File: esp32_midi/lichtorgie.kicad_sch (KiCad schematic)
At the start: 64 parts

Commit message: Updated pcb
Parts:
- renumbered D26 to D?

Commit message: Started work on PCB
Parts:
- added D? (x8): WS2812B, LED_SMD:LED_WS2812B_PLCC4_5.0x5.0mm_P3.2mm, symbol LED:WS2812B
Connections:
- net VDD: now also D?.1 (VDD), D?.1 (VDD), D?.1 (VDD), D?.1 (VDD), D?.1 (VDD), D?.1 (VDD), D?.1 (VDD), D?.1 (VDD)
- net VSS: now also D?.3 (VSS), D?.3 (VSS), D?.3 (VSS), D?.3 (VSS), D?.3 (VSS), D?.3 (VSS), D?.3 (VSS), D?.3 (VSS)
- net at D?.2 (DOUT): now also D?.4 (DIN)
- new net: D?.2 (DOUT), D?.4 (DIN) (x7)

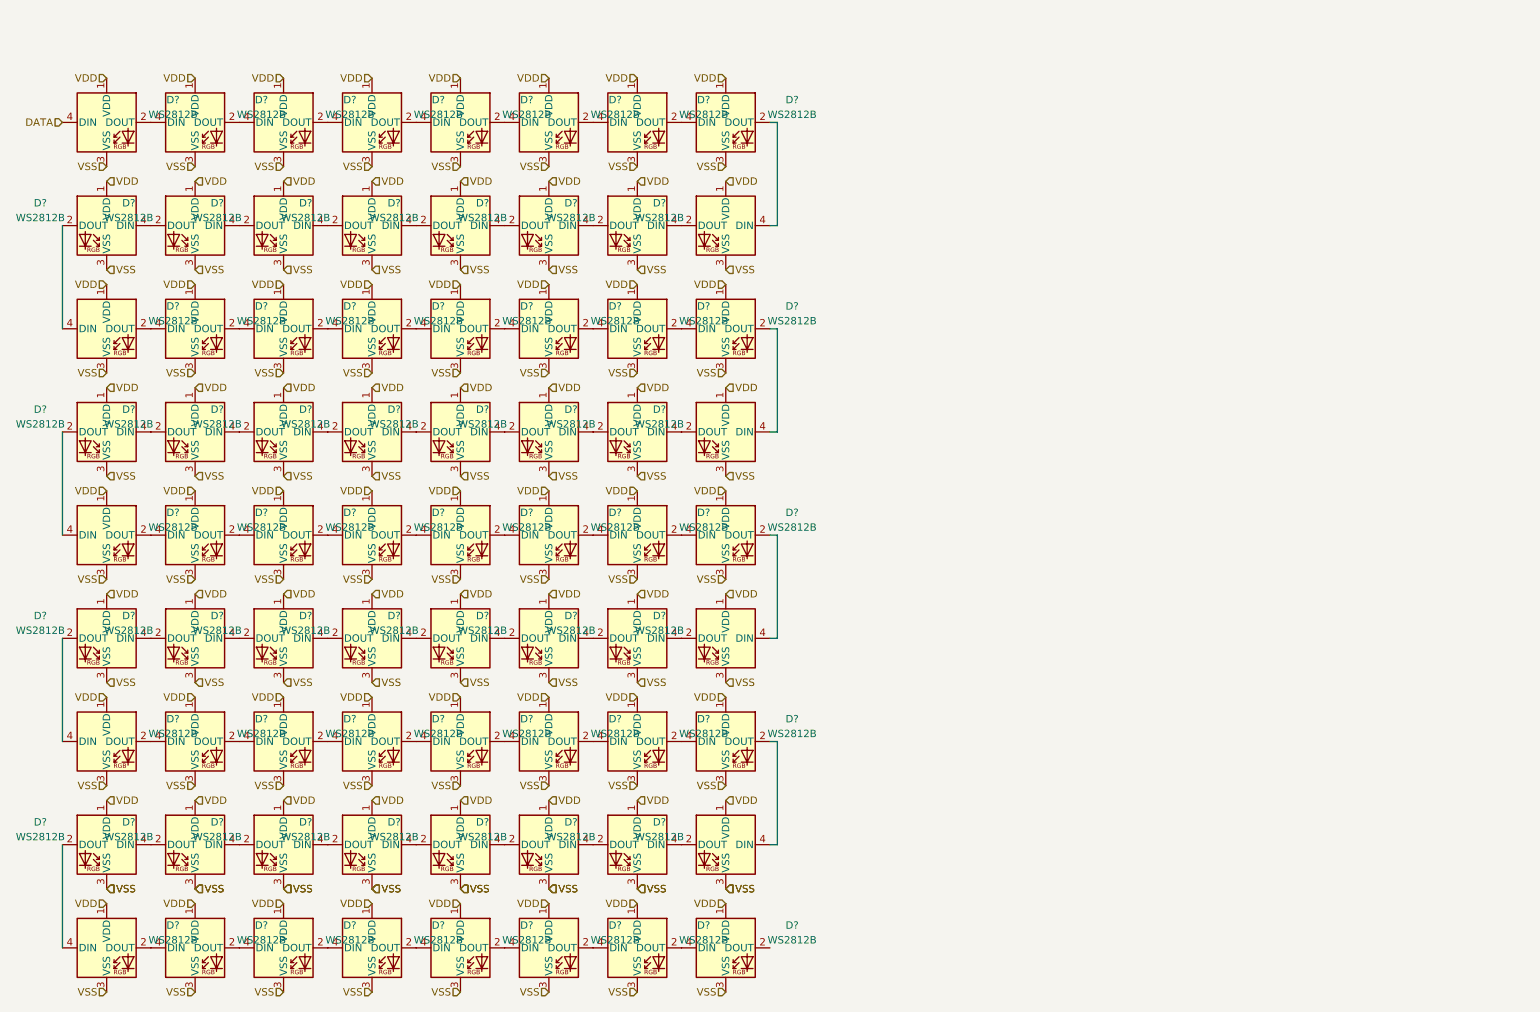
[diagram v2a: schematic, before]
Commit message: improve component spacing, add more LEDs
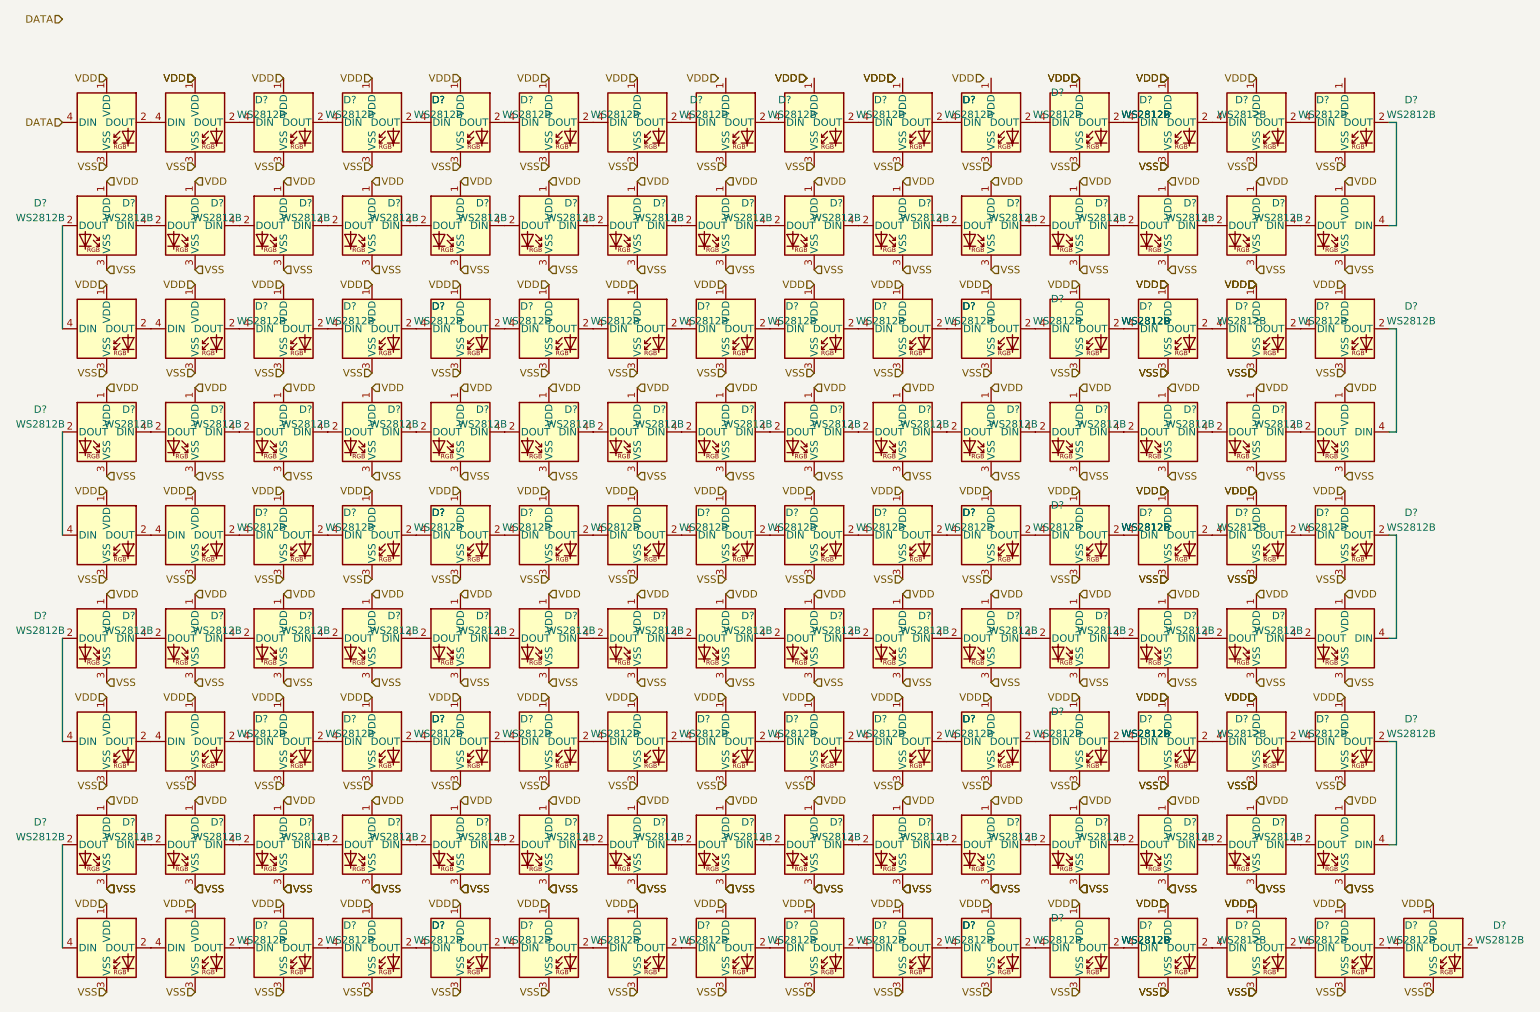
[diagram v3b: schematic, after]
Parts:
- added D? (x64): WS2812B, LED_SMD:LED_WS2812B_PLCC4_5.0x5.0mm_P3.2mm, symbol LED:WS2812B
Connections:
- net VDD: now also D?.1 (VDD), D?.1 (VDD), D?.1 (VDD), D?.1 (VDD), D?.1 (VDD), D?.1 (VDD), D?.1 (VDD), D?.1 (VDD), D?.1 (VDD), D?.1 (VDD), D?.1 (VDD), D?.1 (VDD), D?.1 (VDD), D?.1 (VDD), D?.1 (VDD), D?.1 (VDD), D?.1 (VDD), D?.1 (VDD), D?.1 (VDD), D?.1 (VDD), D?.1 (VDD), D?.1 (VDD), D?.1 (VDD), D?.1 (VDD), D?.1 (VDD), D?.1 (VDD), D?.1 (VDD), D?.1 (VDD), D?.1 (VDD), D?.1 (VDD), D?.1 (VDD), D?.1 (VDD), D?.1 (VDD), D?.1 (VDD), D?.1 (VDD), D?.1 (VDD), D?.1 (VDD), D?.1 (VDD), D?.1 (VDD), D?.1 (VDD), D?.1 (VDD), D?.1 (VDD), D?.1 (VDD), D?.1 (VDD), D?.1 (VDD), D?.1 (VDD), D?.1 (VDD), D?.1 (VDD), D?.1 (VDD), D?.1 (VDD), D?.1 (VDD), D?.1 (VDD), D?.1 (VDD), D?.1 (VDD), D?.1 (VDD), D?.1 (VDD), D?.1 (VDD), D?.1 (VDD), D?.1 (VDD), D?.1 (VDD), D?.1 (VDD), D?.1 (VDD); no longer D?.1 (VDD), D?.1 (VDD), D?.1 (VDD)
- net VSS: now also D?.3 (VSS), D?.3 (VSS), D?.3 (VSS), D?.3 (VSS), D?.3 (VSS), D?.3 (VSS), D?.3 (VSS), D?.3 (VSS), D?.3 (VSS), D?.3 (VSS), D?.3 (VSS), D?.3 (VSS), D?.3 (VSS), D?.3 (VSS), D?.3 (VSS), D?.3 (VSS), D?.3 (VSS), D?.3 (VSS), D?.3 (VSS), D?.3 (VSS), D?.3 (VSS), D?.3 (VSS), D?.3 (VSS), D?.3 (VSS), D?.3 (VSS), D?.3 (VSS), D?.3 (VSS), D?.3 (VSS), D?.3 (VSS), D?.3 (VSS), D?.3 (VSS), D?.3 (VSS), D?.3 (VSS), D?.3 (VSS), D?.3 (VSS), D?.3 (VSS), D?.3 (VSS), D?.3 (VSS), D?.3 (VSS), D?.3 (VSS), D?.3 (VSS), D?.3 (VSS), D?.3 (VSS), D?.3 (VSS), D?.3 (VSS), D?.3 (VSS), D?.3 (VSS), D?.3 (VSS), D?.3 (VSS), D?.3 (VSS), D?.3 (VSS), D?.3 (VSS), D?.3 (VSS), D?.3 (VSS), D?.3 (VSS), D?.3 (VSS), D?.3 (VSS), D?.3 (VSS), D?.3 (VSS), D?.3 (VSS), D?.3 (VSS), D?.3 (VSS), D?.3 (VSS), D?.3 (VSS)
- net at D?.2 (DOUT): now also D?.4 (DIN); no longer D?.4 (DIN) (x19)
- net at D?.4 (DIN): now also D?.2 (DOUT); no longer D?.2 (DOUT) (x44)
- net at D?.2 (DOUT): now also D?.4 (DIN)
- new net: D?.2 (DOUT), D?.4 (DIN) (x63)
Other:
- moved on the sheet: D?

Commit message: Finished
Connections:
- net VDD: now also D?.1 (VDD), D?.1 (VDD), D?.1 (VDD), D?.1 (VDD), D?.1 (VDD)
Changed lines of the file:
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@@
     (effects (font (size 1.27 1.27)) (justify right))
   )
-  (hierarchical_label "VDD" (shape input) (at 165.1 19.05 180) (fields_autoplaced)
+  (hierarchical_label "VDD" (shape input) (at 166.37 19.05 180) (fields_autoplaced)
     (effects (font (size 1.27 1.27)) (justify right))
   )
@@
     (effects (font (size 1.27 1.27)) (justify left))
   )
-  (hierarchical_label "VDD" (shape input) (at 180.34 19.05 180) (fields_autoplaced)
+  (hierarchical_label "VDD" (shape input) (at 181.61 19.05 180) (fields_autoplaced)
+    (effects (font (size 1.27 1.27)) (justify right))
+  )
+  (hierarchical_label "VDD" (shape input) (at 242.57 19.05 180) (fields_autoplaced)
     (effects (font (size 1.27 1.27)) (justify right))
   )
@@
     (effects (font (size 1.27 1.27)) (justify right))
   )
-  (hierarchical_label "VDD" (shape input) (at 149.86 19.05 180) (fields_autoplaced)
-    (effects (font (size 1.27 1.27)) (justify right))
-  )
   (hierarchical_label "VDD" (shape input) (at 227.33 161.29 180) (fields_autoplaced)
     (effects (font (size 1.27 1.27)) (justify right))
@@
     (effects (font (size 1.27 1.27)) (justify left))
   )
-  (hierarchical_label "VDD" (shape input) (at 165.1 19.05 180) (fields_autoplaced)
-    (effects (font (size 1.27 1.27)) (justify right))
-  )
   (hierarchical_label "VDD" (shape input) (at 151.13 161.29 180) (fields_autoplaced)
     (effects (font (size 1.27 1.27)) (justify right))
@@
     (effects (font (size 1.27 1.27)) (justify right))
   )
-  (hierarchical_label "VDD" (shape input) (at 134.62 19.05 180) (fields_autoplaced)
+  (hierarchical_label "VDD" (shape input) (at 135.89 19.05 180) (fields_autoplaced)
     (effects (font (size 1.27 1.27)) (justify right))
   )
@@
     (effects (font (size 1.27 1.27)) (justify right))
   )
-  (hierarchical_label "VDD" (shape input) (at 149.86 19.05 180) (fields_autoplaced)
-    (effects (font (size 1.27 1.27)) (justify right))
-  )
+  (hierarchical_label "VDD" (shape input) (at 151.13 19.05 180) (fields_autoplaced)
+    (effects (font (size 1.27 1.27)) (justify right))
+  )

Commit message: First load of bug fixes
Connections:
- no-connect marks 0 -> 1

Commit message: Update parts numbers
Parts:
- D? (x136): Field-1 (none) -> ${DNP}
